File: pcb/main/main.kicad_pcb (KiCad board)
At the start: 2 copper layers, 29.4 x 98.3 mm, 54 parts, among them J1 Conn_01x04, J2 USB_B, J3 Serial, J4 STLink, J5 RJ45, J6 SELECT, J7 READ, J8 TRACKBALL, SW5 RST_SW, SW6 BOOT0, SW7 BOOT1, U1 3.3v regul, U2 STM32F103C8Tx, Y1 32.768kHz, Y2 8MHz

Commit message: fix pcb
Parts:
- removed D5, D6, D7: LED, LED_SMD:LED_1206_3216Metric
- removed G*** (x2): LOGO, folivora:logo
- removed JP10, JP12, JP14, JP16, JP9: R, Jumper:SolderJumper-2_P1.3mm_Open_TrianglePad1.0x1.5mm
- removed JP11, JP13, JP15, JP17: L, Jumper:SolderJumper-2_P1.3mm_Open_TrianglePad1.0x1.5mm
- removed SW5: RST_SW, Button_Switch_THT:SW_Tactile_SPST_Angled_PTS645Vx31-2LFS
- removed SW6: BOOT0, Button_Switch_THT:SW_CuK_OS102011MA1QN1_SPDT_Angled
- removed SW7: BOOT1, Button_Switch_THT:SW_CuK_OS102011MA1QN1_SPDT_Angled
- added C12: C, Capacitor_SMD:C_0402_1005Metric, F.Cu at (25.0, -43.8)
- added C13: 1uF, Capacitor_SMD:C_0402_1005Metric, F.Cu at (12.1, -39.4)
- added C14: 0.1uF, Capacitor_SMD:C_0402_1005Metric, F.Cu at (12.1, -40.6)
- added C15: 0.1uF, Capacitor_SMD:C_0402_1005Metric, F.Cu at (8.26, -36.8)
- added C16: 1uF, Capacitor_SMD:C_0402_1005Metric, F.Cu at (32.4, -46.4)
- added C17: 1uF, Capacitor_SMD:C_0402_1005Metric, F.Cu at (17.1, -8.89)
- added C18: 0.1uF, Capacitor_SMD:C_0402_1005Metric, F.Cu at (17.1, -7.62)
- added C19: 0.1uF, Capacitor_SMD:C_0402_1005Metric, F.Cu at (14.6, -5.08)
- added C20: 1uF, Capacitor_SMD:C_0402_1005Metric, F.Cu at (13.3, -5.08)
- added C21: 0.1uF, Capacitor_SMD:C_0402_1005Metric, F.Cu at (1.91, -34.3)
- added D1: SBD, Diode_SMD:D_SOD-123, F.Cu at (15.9, -36.8)
- added D2: Error, LED_SMD:LED_0603_1608Metric, F.Cu at (1.91, -67.9)
- added D3: Status, LED_SMD:LED_0603_1608Metric, F.Cu at (1.91, -66.0)
- added D4: SBD, Diode_SMD:D_SOD-123, F.Cu at (17.1, -11.4)
- added J10: COL4, Connector_JST:JST_PH_B4B-PH-K_1x04_P2.00mm_Vertical, F.Cu at (28.9, -34.9)
- added J11: COL6, Connector_JST:JST_PH_B3B-PH-K_1x03_P2.00mm_Vertical, F.Cu at (38.9, -34.9)
- added J12: OLED, folivora:OLED, F.Cu at (6.35, -8.89)
- added J13: Conn_01x05_Female, Connector_JST:JST_PH_B5B-PH-K_1x05_P2.00mm_Vertical, F.Cu at (34.9, -11.4)
- added J9: COL3, Connector_JST:JST_PH_B4B-PH-K_1x04_P2.00mm_Vertical, F.Cu at (28.9, -29.2)
- added JP1: OLED_1_F, Jumper:SolderJumper-2_P1.3mm_Open_Pad1.0x1.5mm, F.Cu at (2.54, -12.7)
- added R10: 10k, Resistor_SMD:R_0402_1005Metric, B.Cu at (36.8, -20.3)
- added R11: 10k, Resistor_SMD:R_0402_1005Metric, B.Cu at (34.9, -20.3)
- added R12: 10k, Resistor_SMD:R_0402_1005Metric, B.Cu at (40.6, -26.0)
- added R13: 10k, Resistor_SMD:R_0402_1005Metric, B.Cu at (38.7, -26.0)
- added R14: 10k, Resistor_SMD:R_0402_1005Metric, B.Cu at (36.8, -26.0)
- added R15: 10k, Resistor_SMD:R_0402_1005Metric, B.Cu at (34.9, -26.0)
- added R16: 10k, Resistor_SMD:R_0402_1005Metric, B.Cu at (28.6, -31.8)
- added R17: 10k, Resistor_SMD:R_0402_1005Metric, B.Cu at (26.7, -31.8)
- added R18: 10k, Resistor_SMD:R_0402_1005Metric, B.Cu at (24.8, -31.8)
- added R19: 10k, Resistor_SMD:R_0402_1005Metric, B.Cu at (22.9, -31.8)
- added R20: 10k, Resistor_SMD:R_0402_1005Metric, B.Cu at (34.9, -37.5)
- added R21: 10k, Resistor_SMD:R_0402_1005Metric, B.Cu at (36.8, -37.5)
- added R22: 10k, Resistor_SMD:R_0402_1005Metric, B.Cu at (38.7, -37.5)
- added R23: 10k, Resistor_SMD:R_0402_1005Metric, B.Cu at (22.9, -37.5)
- added R24: 10, Resistor_SMD:R_0402_1005Metric, F.Cu at (20.3, -65.2)
- added R25: 10k, Resistor_SMD:R_0402_1005Metric, B.Cu at (24.8, -37.5)
- added R26: 10k, Resistor_SMD:R_0402_1005Metric, B.Cu at (26.7, -37.5)
- added R27: 10k, Resistor_SMD:R_0402_1005Metric, B.Cu at (28.6, -37.5)
- added R28: 10k, Resistor_SMD:R_0402_1005Metric, B.Cu at (22.9, -26.0)
- added R29: 10k, Resistor_SMD:R_0402_1005Metric, B.Cu at (24.8, -26.0)
- added R30: 10k, Resistor_SMD:R_0402_1005Metric, B.Cu at (26.7, -26.0)
- added R31: 10k, Resistor_SMD:R_0402_1005Metric, B.Cu at (28.6, -26.0)
- added R32: 10k, Resistor_SMD:R_0402_1005Metric, B.Cu at (34.9, -31.8)
- added R33: 10k, Resistor_SMD:R_0402_1005Metric, B.Cu at (36.8, -31.8)
- added R34: 10k, Resistor_SMD:R_0402_1005Metric, B.Cu at (38.7, -31.8)
- added R35: 10k, Resistor_SMD:R_0402_1005Metric, B.Cu at (22.9, -20.3)
- added R36: 10k, Resistor_SMD:R_0402_1005Metric, B.Cu at (24.8, -20.3)
- added R37: 10k, Resistor_SMD:R_0402_1005Metric, B.Cu at (26.7, -20.3)
- added R38: 10k, Resistor_SMD:R_0402_1005Metric, B.Cu at (28.6, -20.3)
- added R39: R, Resistor_SMD:R_0402_1005Metric, F.Cu at (22.9, -3.81)
- added R40: 10, Resistor_SMD:R_0402_1005Metric, F.Cu at (20.3, -64.1)
- added R41: 5.1k, Resistor_SMD:R_0402_1005Metric, F.Cu at (17.8, -69.8)
- added R8: 10k, Resistor_SMD:R_0402_1005Metric, B.Cu at (40.6, -20.3)
- added R9: 10k, Resistor_SMD:R_0402_1005Metric, B.Cu at (38.7, -20.3)
- added REF_M1: MountingHole_2.2mm_M2, MountingHole:MountingHole_2.2mm_M2, F.Cu at (41.9, -2.54)
- added REF_M2: MountingHole_2.2mm_M2, MountingHole:MountingHole_2.2mm_M2, F.Cu at (10.8, -2.54)
- added REF_M3: MountingHole_2.2mm_M2, MountingHole:MountingHole_2.2mm_M2, F.Cu at (2.54, -2.54)
- added REF_M4: MountingHole_2.2mm_M2, MountingHole:MountingHole_2.2mm_M2, F.Cu at (10.8, -45.7)
- added REF_M5: MountingHole_2.2mm_M2, MountingHole:MountingHole_2.2mm_M2, F.Cu at (2.54, -45.7)
- added REF_M6: MountingHole_2.2mm_M2, MountingHole:MountingHole_2.2mm_M2, F.Cu at (41.9, -72.4)
- added REF_M7: MountingHole_2.2mm_M2, MountingHole:MountingHole_2.2mm_M2, F.Cu at (2.54, -72.4)
- added SW1: SW_SPDT, Button_Switch_SMD:SW_SPDT_PCM12, F.Cu at (2.54, -29.2)
- added SW2: SW_SPDT, Button_Switch_SMD:SW_SPDT_PCM12, F.Cu at (2.54, -19.7)
- added SW3: RESET, Button_Switch_SMD:SW_SPST_EVQP7C, F.Cu at (1.91, -38.1)
- added U3: PCA9306DC1, Package_SO:VSSOP-8_2.3x2mm_P0.5mm, F.Cu at (22.9, -1.91)
- added U4: HT7727, Package_TO_SOT_SMD:SOT-23, F.Cu at (17.1, -5.08)
- C1, C2: value 10uF -> 0.1uF; footprint Capacitor_SMD:C_1206_3216Metric_Pad1.42x1.75mm_HandSolder -> Capacitor_SMD:C_0402_1005Metric
- C10, C11, C9: value 0.1uF -> C; footprint Capacitor_SMD:C_0603_1608Metric_Pad1.05x0.95mm_HandSolder -> Capacitor_SMD:C_0402_1005Metric
- C3: value 12.5pF -> 0.1uF; footprint Capacitor_SMD:C_0603_1608Metric_Pad1.05x0.95mm_HandSolder -> Capacitor_SMD:C_0402_1005Metric
- C4: value 12.5pF[ -> 0.1uF; footprint Capacitor_SMD:C_0603_1608Metric_Pad1.05x0.95mm_HandSolder -> Capacitor_SMD:C_0402_1005Metric
- C5: value 20pF -> 0.1uF; footprint Capacitor_SMD:C_0603_1608Metric_Pad1.05x0.95mm_HandSolder -> Capacitor_SMD:C_0402_1005Metric
- C6: value 20pF -> 1uF; footprint Capacitor_SMD:C_0603_1608Metric_Pad1.05x0.95mm_HandSolder -> Capacitor_SMD:C_0402_1005Metric
- C7: value 10uF -> 10nF; footprint Capacitor_SMD:C_0603_1608Metric_Pad1.05x0.95mm_HandSolder -> Capacitor_SMD:C_0402_1005Metric
- C8: value 0.1uF -> 4.7uF; footprint Capacitor_SMD:C_0603_1608Metric_Pad1.05x0.95mm_HandSolder -> Capacitor_SMD:C_0402_1005Metric
- J1: value Conn_01x04 -> USB_C_Receptacle_USB2.0; footprint Connector_PinSocket_2.54mm:PinSocket_1x04_P2.54mm_Vertical -> Connector_USB:USB_C_Receptacle_HRO_TYPE-C-31-M-12
- J2: value USB_B -> RJ45; footprint Connector_USB:USB_B_OST_USB-B1HSxx_Horizontal -> folivora:RJ45_rev
- J3: value Serial -> RJ45; footprint Connector_PinHeader_2.54mm:PinHeader_1x04_P2.54mm_Vertical -> folivora:RJ45_rev; moved to B.Cu
- J4: value STLink -> Pad; footprint Connector_PinHeader_2.54mm:PinHeader_1x04_P2.54mm_Vertical -> Connector_JST:JST_PH_B4B-PH-K_1x04_P2.00mm_Vertical
- J5: value RJ45 -> Thumb; footprint folivora:RJ45_rev -> Connector_JST:JST_PH_B4B-PH-K_1x04_P2.00mm_Vertical
- J6: value SELECT -> COL1; footprint Connector_PinSocket_2.54mm:PinSocket_1x05_P2.54mm_Vertical -> Connector_JST:JST_PH_B4B-PH-K_1x04_P2.00mm_Vertical
- J7: value READ -> COL5; footprint Connector_PinSocket_2.54mm:PinSocket_1x06_P2.54mm_Vertical -> Connector_JST:JST_PH_B3B-PH-K_1x03_P2.00mm_Vertical
- J8: value TRACKBALL -> COL2; footprint Connector_PinSocket_2.54mm:PinSocket_1x06_P2.54mm_Vertical -> Connector_JST:JST_PH_B4B-PH-K_1x04_P2.00mm_Vertical
- JP2: value L -> OLED_1_B; footprint Jumper:SolderJumper-2_P1.3mm_Open_TrianglePad1.0x1.5mm -> Jumper:SolderJumper-2_P1.3mm_Open_Pad1.0x1.5mm
- JP3: value R -> OLED_2_F; footprint Jumper:SolderJumper-2_P1.3mm_Open_TrianglePad1.0x1.5mm -> Jumper:SolderJumper-2_P1.3mm_Open_Pad1.0x1.5mm
- JP4: value L -> OLED_2_B; footprint Jumper:SolderJumper-2_P1.3mm_Open_TrianglePad1.0x1.5mm -> Jumper:SolderJumper-2_P1.3mm_Open_Pad1.0x1.5mm
- JP5: value R -> OLED_3_F; footprint Jumper:SolderJumper-2_P1.3mm_Open_TrianglePad1.0x1.5mm -> Jumper:SolderJumper-2_P1.3mm_Open_Pad1.0x1.5mm
- JP6: value L -> OLED_3_B; footprint Jumper:SolderJumper-2_P1.3mm_Open_TrianglePad1.0x1.5mm -> Jumper:SolderJumper-2_P1.3mm_Open_Pad1.0x1.5mm
- JP7: value R -> OLED_4_F; footprint Jumper:SolderJumper-2_P1.3mm_Open_TrianglePad1.0x1.5mm -> Jumper:SolderJumper-2_P1.3mm_Open_Pad1.0x1.5mm
- JP8: value L -> OLED_4_B; footprint Jumper:SolderJumper-2_P1.3mm_Open_TrianglePad1.0x1.5mm -> Jumper:SolderJumper-2_P1.3mm_Open_Pad1.0x1.5mm
- R1: footprint Resistor_SMD:R_0603_1608Metric -> Resistor_SMD:R_0402_1005Metric
- R2, R3: value R -> 10M; footprint Resistor_SMD:R_0603_1608Metric -> Resistor_SMD:R_0402_1005Metric
- R4: value 10Mohm -> R; footprint Resistor_SMD:R_0603_1608Metric_Pad1.05x0.95mm_HandSolder -> Resistor_SMD:R_0402_1005Metric
- R5, R6, R7: value 10kohm -> R; footprint Resistor_SMD:R_0603_1608Metric_Pad1.05x0.95mm_HandSolder -> Resistor_SMD:R_0402_1005Metric
- U1: value 3.3v regul -> STM32F401RETx; footprint Package_TO_SOT_SMD:TO-252-3_TabPin2 -> Package_QFP:LQFP-64_10x10mm_P0.5mm
- U2: value STM32F103C8Tx -> NATLINEAR XT1861B332MR-G; footprint Package_QFP:LQFP-48_7x7mm_P0.5mm -> Package_TO_SOT_SMD:SOT-23
- Y1: value 32.768kHz -> Crystal_8MHz; footprint Crystal:Crystal_SMD_3215-2Pin_3.2x1.5mm -> Crystal:Crystal_SMD_2520-4Pin_2.5x2.0mm
- Y2: value 8MHz -> Crystal_32.768MHz; footprint Crystal:Crystal_SMD_Abracon_ABM3-2Pin_5.0x3.2mm -> Crystal:Crystal_SMD_2520-4Pin_2.5x2.0mm
- moved R5 153.8 mm to (4.45, -67.9), turned to 180 degrees
- moved C7 137.6 mm to (30.3, -46.4), turned to 180 degrees
- moved J1 135.9 mm to (11.4, -70.5), turned to 180 degrees
- moved R6 124.0 mm to (4.45, -66.0), turned to 180 degrees
- moved R1 120.9 mm to (3.17, -42.5)
- moved R2 117.9 mm to (28.2, -46.1), turned to 0 degrees
- moved R3 115.6 mm to (22.5, -46.4), turned to 0 degrees
- moved C8 113.0 mm to (37.5, -57.0)
- moved C11 102.9 mm to (19.9, -43.8), turned to 90 degrees
- moved C2 98.1 mm to (24.8, -61.6), turned to 0 degrees
- moved C5 94.9 mm to (21.0, -50.0), turned to 90 degrees
- moved C3 94.6 mm to (36.2, -50.8), turned to 270 degrees
- moved C1 93.5 mm to (36.2, -57.8), turned to 270 degrees
- moved C10 92.9 mm to (31.0, -43.8)
- moved J5 92.9 mm to (40.9, -17.8), turned to 180 degrees
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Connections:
- C1 pad 1: +5V -> +3V3
- C10 pad 1: +3V3 -> /XTAL1B
- C11 pad 1: +3V3 -> /XTAL2A
- C3 pad 1: GND -> +3V3
- C3 pad 2: /XTAL_C -> GND
- C4 pad 1: GND -> +3V3
- C4 pad 2: /XTAL_D -> GND
- C5 pad 1: GND -> +3V3
- C5 pad 2: /XTAL_A -> GND
- C6 pad 1: GND -> +3V3
- C6 pad 2: /XTAL_B -> GND
- C7 pad 1: /RST -> +3V3
- C8 pad 1: +3V3 -> Net-(C8-Pad1)
- C9 pad 1: +3V3 -> /XTAL1A
- J2 pad 1: /USB_1 -> /SCLK
- J2 pad 2: /USB_2 -> /MISO
- J2 pad 3: /USB_3 -> /MOSI
- J2 pad 4: /USB_4 -> VBUS
- J2 pad 5: GND -> VBUS
- J3 pad 1: GND -> /SCLK
- J3 pad 2: /RX -> /MOSI
- J3 pad 3: /TX -> /MISO
- J3 pad 4: +3V3 -> VBUS
- J4 pad 1: GND -> Net-(J4-Pad1)
- J4 pad 2: /SWCLK -> Net-(J4-Pad2)
- J4 pad 3: /SWDIO -> Net-(J4-Pad3)
- J4 pad 4: +3V3 -> Net-(J4-Pad4)
- J5 pad 1: GND -> Net-(J5-Pad1)
- J5 pad 2: GND -> Net-(J5-Pad2)
- J5 pad 3: /SCK -> Net-(J5-Pad3)
- J5 pad 4: /MOSI -> Net-(J5-Pad4)
- J6 pad 1: /SELECT0 -> Net-(J6-Pad1)
- J6 pad 2: /SELECT1 -> Net-(J6-Pad2)
- J6 pad 3: /SELECT2 -> Net-(J6-Pad3)
- J6 pad 4: /SELECT3 -> Net-(J6-Pad4)
- J7 pad 1: /READ0 -> Net-(J7-Pad1)
- J7 pad 2: /READ1 -> Net-(J7-Pad2)
- J7 pad 3: /READ2 -> Net-(J7-Pad3)
- J8 pad 1: +3V3 -> Net-(J8-Pad1)
- J8 pad 2: /UP -> Net-(J8-Pad2)
- J8 pad 3: /DOWN -> Net-(J8-Pad3)
- J8 pad 4: /RIGHT -> Net-(J8-Pad4)
- JP2 pad 1: /D- -> /SDA
- JP2 pad 2: /USB_1 -> /OLED1
- JP3 pad 1: +5V -> +3V3
- JP3 pad 2: /USB_1 -> /OLED2
- JP4 pad 1: +5V -> /SCL
- JP4 pad 2: /USB_2 -> /OLED2
- JP5 pad 1: /D- -> /SCL
- JP5 pad 2: /USB_2 -> /OLED3
- JP6 pad 1: GND -> +3V3
- JP6 pad 2: /USB_3 -> /OLED3
- JP7 pad 1: /D+ -> /SDA
- JP7 pad 2: /USB_3 -> /OLED4
- JP8 pad 1: /D+ -> GND
- JP8 pad 2: /USB_4 -> /OLED4
- R1 pad 2: Net-(D5-Pad2) -> Net-(C21-Pad2)
- R2 pad 1: +3V3 -> /XTAL1A
- R2 pad 2: Net-(D6-Pad2) -> /XTAL1B
- R3 pad 1: +3V3 -> /XTAL2A
- R3 pad 2: Net-(D7-Pad2) -> /XTAL2B
- R4 pad 1: /XTAL_B -> +3V3
- R4 pad 2: /XTAL_A -> Net-(R4-Pad2)
- R5 pad 1: /RST -> +3V3
- R5 pad 2: +3V3 -> Net-(D2-Pad2)
- R6 pad 1: Net-(R6-Pad1) -> +3V3
- R6 pad 2: /BOOT0 -> Net-(D3-Pad2)
- R7 pad 1: Net-(R7-Pad1) -> +3V3
- R7 pad 2: /BOOT1 -> Net-(R7-Pad2)
- U1 pad 1: +5V -> +3V3
- U1 pad 2: GND -> /XTAL2A
- U1 pad 3: +3V3 -> /XTAL2B
- U2 pad 1: +3V3 -> VBUS
- U2 pad 2: Net-(U2-Pad2) -> GND
- U2 pad 3: /XTAL_C -> +3V3
- Y1 pad 1: /XTAL_D -> /XTAL1B
- Y1 pad 2: /XTAL_C -> GND
- Y2 pad 1: /XTAL_B -> /XTAL2B
- Y2 pad 2: /XTAL_A -> GND
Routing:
- net +3V3: track 175.5 -> 265.0 mm, vias 7 -> 3
- net VBUS: track 0.00 -> 85.0 mm
- net Net-(J5-Pad3): track 0.00 -> 71.3 mm, vias 0 -> 1
- net Net-(J5-Pad2): track 0.00 -> 69.3 mm, vias 0 -> 1
- net Net-(J5-Pad1): track 0.00 -> 61.9 mm, vias 0 -> 1
- net Net-(J5-Pad4): track 0.00 -> 61.8 mm
- net /SDA: track 22.1 -> 80.4 mm
- net /SCL: track 17.7 -> 75.3 mm
- net Net-(J7-Pad3): track 0.00 -> 54.1 mm, vias 0 -> 2
- net Net-(J7-Pad2): track 0.00 -> 50.7 mm, vias 0 -> 2
- net Net-(J4-Pad1): track 0.00 -> 50.4 mm
- net Net-(J4-Pad2): track 0.00 -> 50.2 mm
- net Net-(J4-Pad3): track 0.00 -> 49.6 mm
- net Net-(J8-Pad3): track 0.00 -> 46.5 mm, vias 0 -> 1
- net /RST: track 45.7 -> 0.00 mm, vias 2 -> 0
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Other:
- board size 29.4 x 98.3 mm -> 44.5 x 74.9 mm

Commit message: pcb update
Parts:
- removed JP1: OLED_1_F, Jumper:SolderJumper-2_P1.3mm_Open_Pad1.0x1.5mm
- removed JP2: OLED_1_B, Jumper:SolderJumper-2_P1.3mm_Open_Pad1.0x1.5mm
- removed JP3: OLED_2_F, Jumper:SolderJumper-2_P1.3mm_Open_Pad1.0x1.5mm
- removed JP4: OLED_2_B, Jumper:SolderJumper-2_P1.3mm_Open_Pad1.0x1.5mm
- removed JP5: OLED_3_F, Jumper:SolderJumper-2_P1.3mm_Open_Pad1.0x1.5mm
- removed JP6: OLED_3_B, Jumper:SolderJumper-2_P1.3mm_Open_Pad1.0x1.5mm
- removed JP7: OLED_4_F, Jumper:SolderJumper-2_P1.3mm_Open_Pad1.0x1.5mm
- removed JP8: OLED_4_B, Jumper:SolderJumper-2_P1.3mm_Open_Pad1.0x1.5mm
- added J14: OLED, folivora:OLED, F.Cu at (6.35, -8.89)
- J12: moved to B.Cu
- R10, R11, R12, R13, R14, R15, R16, R17, R18, R19, R20, R21, R22, R23, R25, R26, R27, R28, R29, R30, R31, R32, R33, R34, R35, R36, R37, R38, R8, R9: moved to F.Cu
- moved C16 6.90 mm to (37.0, -51.5)
- moved C12 6.90 mm to (29.6, -48.9)
- moved C4 6.90 mm to (27.5, -53.4)
- moved C5 6.90 mm to (25.6, -55.1)
- moved C9 6.90 mm to (30.7, -48.9)
- moved R3 6.90 mm to (27.1, -51.5)
- moved Y1 6.90 mm to (33.2, -48.9)
- moved Y2 6.90 mm to (27.1, -48.9)
- moved C1 6.90 mm to (40.8, -62.9)
- moved C10 6.90 mm to (35.6, -48.9)
- moved C3 6.90 mm to (40.8, -55.9)
- moved C8 6.90 mm to (42.1, -62.1)
- moved C7 6.90 mm to (34.9, -51.5)
- moved R2 6.90 mm to (32.8, -51.2)
- moved U1 6.90 mm to (33.2, -59.1)
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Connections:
- J1 pad A8: Net-(J1-PadA8) -> (no net)
- J1 pad B8: Net-(J1-PadB8) -> (no net)
- J12 pad 1: /OLED1 -> GND
- J12 pad 2: /OLED2 -> +3V3
- J12 pad 3: /OLED3 -> /SCL
- J12 pad 4: /OLED4 -> /SDA
- J13 pad 3: Net-(J13-Pad3) -> (no net)
- U1 pad 24: Net-(U1-Pad24) -> (no net)
- U1 pad 4: Net-(U1-Pad4) -> (no net)
- U1 pad 41: /TSS -> (no net)
- U1 pad 54: Net-(U1-Pad54) -> (no net)
- U1 pad 57: Net-(U1-Pad57) -> (no net)
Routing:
- net +3V3: track 265.0 -> 345.4 mm, vias 3 -> 8
- net /CONFIG: track 44.8 -> 70.8 mm
- net Net-(J9-Pad2): track 20.8 -> 39.2 mm
- net /SDA: track 80.4 -> 97.4 mm
- net Net-(J9-Pad1): track 22.5 -> 38.6 mm, vias 2 -> 1
- net Net-(J10-Pad4): track 30.6 -> 46.1 mm, vias 1 -> 2
- net Net-(J6-Pad3): track 37.1 -> 52.1 mm, vias 0 -> 1
- net Net-(J9-Pad4): track 25.0 -> 39.7 mm
- net Net-(J11-Pad3): track 32.1 -> 46.6 mm
- net Net-(J6-Pad4): track 45.1 -> 59.3 mm, vias 0 -> 1
- net Net-(J8-Pad1): track 38.7 -> 52.6 mm, vias 2 -> 1
- net Net-(J7-Pad3): track 54.1 -> 67.6 mm, vias 2 -> 1
- net Net-(J6-Pad2): track 39.2 -> 51.0 mm, vias 0 -> 1
- net Net-(J4-Pad4): track 36.8 -> 48.5 mm, vias 0 -> 1
- net /MISO: track 49.5 -> 60.3 mm
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
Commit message: redesign pcb
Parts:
- removed J10: COL4, Connector_JST:JST_PH_B4B-PH-K_1x04_P2.00mm_Vertical
- removed J11: COL6, Connector_JST:JST_PH_B3B-PH-K_1x03_P2.00mm_Vertical
- removed J7: COL5, Connector_JST:JST_PH_B3B-PH-K_1x03_P2.00mm_Vertical
- removed J8: COL2, Connector_JST:JST_PH_B4B-PH-K_1x04_P2.00mm_Vertical
- removed J9: COL3, Connector_JST:JST_PH_B4B-PH-K_1x04_P2.00mm_Vertical
- removed R10, R11, R12, R13, R14, R15, R16, R17, R18, R19, R20, R21, R22, R23, R25, R26, R27, R28, R29, R30, R31, R32, R33, R34, R35, R36, R37, R38, R8, R9: 10k, Resistor_SMD:R_0402_1005Metric
- removed R3: 10M, Resistor_SMD:R_0402_1005Metric
- removed REF_M7: MountingHole_2.2mm_M2, MountingHole:MountingHole_2.2mm_M2
- added C22: 0.1uF, Capacitor_SMD:C_0402_1005Metric, F.Cu at (6.35, -24.8)
- added C23: 0.1uF, Capacitor_SMD:C_0402_1005Metric, F.Cu at (5.24, -34.3)
- added C24: 0.1uF, Capacitor_SMD:C_0402_1005Metric, F.Cu at (27.9, -3.81)
- added C25: 0.1uF, Capacitor_SMD:C_0402_1005Metric, F.Cu at (21.6, -3.17)
- added D5: LED_USB, LED_SMD:LED_0603_1608Metric, F.Cu at (7.24, -46.4)
- added F1: Polyfuse, Fuse:Fuse_0603_1608Metric, F.Cu at (14.6, -29.8)
- added REF_M1: MountingHole_2.2mm_M2, MountingHole:MountingHole_2.2mm_M2, F.Cu at (17.8, -31.1)
- added REF_M1: MountingHole_2.2mm_M2, MountingHole:MountingHole_2.2mm_M2, F.Cu at (17.8, -2.54)
- J13: value Conn_01x05_Female -> trackball
- J4: value Pad -> STLink; footprint Connector_JST:JST_PH_B4B-PH-K_1x04_P2.00mm_Vertical -> Connector_PinHeader_1.27mm:PinHeader_2x07_P1.27mm_Vertical
- J5: value Thumb -> ROW; footprint Connector_JST:JST_PH_B4B-PH-K_1x04_P2.00mm_Vertical -> Connector_JST:JST_PH_B5B-PH-K_1x05_P2.00mm_Vertical
- J6: value COL1 -> COL; footprint Connector_JST:JST_PH_B4B-PH-K_1x04_P2.00mm_Vertical -> Connector_JST:JST_PH_B6B-PH-K_1x06_P2.00mm_Vertical
- R2: value 10M -> R; footprint Resistor_SMD:R_0402_1005Metric -> Resistor_SMD:R_0201_0603Metric_Pad0.64x0.40mm_HandSolder
- moved C12 41.0 mm to (26.0, -8.10), turned to 180 degrees
- moved C4 40.8 mm to (29.1, -12.6)
- moved C9 40.3 mm to (30.9, -8.59), turned to 270 degrees
- moved C10 39.7 mm to (35.8, -9.23)
- moved Y1 39.7 mm to (33.4, -9.23)
- moved C16 39.6 mm to (15.5, -18.2), turned to 180 degrees
- moved C1 39.1 mm to (41.0, -23.8)
- moved C3 39.1 mm to (41.0, -16.8)
- moved C5 39.1 mm to (25.7, -16.0)
- moved C7 39.1 mm to (35.1, -12.4)
- moved C8 39.1 mm to (42.2, -23.0)
- moved C2 39.1 mm to (29.5, -27.6)
- moved U1 39.1 mm to (33.4, -20.0)
- moved Y2 38.3 mm to (26.0, -10.6), turned to 90 degrees
- moved C6 36.1 mm to (35.1, -11.4), turned to 180 degrees
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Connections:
- C13 pad 1: VBUS -> Net-(C13-Pad1)
- C14 pad 1: VBUS -> Net-(C13-Pad1)
- C17 pad 1: VBUS -> Net-(C13-Pad1)
- C18 pad 1: VBUS -> Net-(C13-Pad1)
- C21 pad 2: Net-(C21-Pad2) -> /NRST
- D1 pad 1: VBUS -> Net-(C13-Pad1)
- D4 pad 1: VBUS -> Net-(C13-Pad1)
- J4 pad 1: Net-(J4-Pad1) -> (no net)
- J4 pad 2: Net-(J4-Pad2) -> (no net)
- J4 pad 3: Net-(J4-Pad3) -> +3V3
- J4 pad 4: Net-(J4-Pad4) -> /SWDIO
- J5 pad 1: Net-(J5-Pad1) -> /ROW1
- J5 pad 2: Net-(J5-Pad2) -> /ROW2
- J5 pad 3: Net-(J5-Pad3) -> /ROW3
- J5 pad 4: Net-(J5-Pad4) -> /ROW4
- J6 pad 1: Net-(J6-Pad1) -> /COL1
- J6 pad 2: Net-(J6-Pad2) -> /COL2
- J6 pad 3: Net-(J6-Pad3) -> /COL3
- J6 pad 4: Net-(J6-Pad4) -> /COL4
- R1 pad 2: Net-(C21-Pad2) -> /NRST
- R2 pad 1: /XTAL1A -> VBUS
- R2 pad 2: /XTAL1B -> Net-(D5-Pad2)
- SW2 pad 2: /CONFIG -> /BOOT1
- SW3 pad 2: Net-(C21-Pad2) -> /NRST
- U1 pad 10: Net-(J9-Pad2) -> (no net)
- U1 pad 11: Net-(J9-Pad1) -> (no net)
- U1 pad 14: Net-(J6-Pad1) -> (no net)
- U1 pad 15: Net-(J6-Pad2) -> (no net)
- U1 pad 16: Net-(J6-Pad3) -> /TX
- U1 pad 17: Net-(J6-Pad4) -> /RX
- U1 pad 20: /SS -> (no net)
- U1 pad 21: /SCLK -> (no net)
- U1 pad 22: /MISO -> (no net)
- U1 pad 23: /MOSI -> (no net)
- U1 pad 25: Net-(J4-Pad4) -> (no net)
- U1 pad 26: Net-(J8-Pad1) -> (no net)
- U1 pad 27: Net-(J8-Pad2) -> (no net)
- U1 pad 28: Net-(J8-Pad3) -> /BOOT1
- U1 pad 29: Net-(J10-Pad3) -> (no net)
- U1 pad 33: Net-(J10-Pad4) -> /ROW1
- U1 pad 34: Net-(J11-Pad1) -> /ROW2
- U1 pad 35: Net-(J11-Pad2) -> /ROW3
- U1 pad 36: Net-(J11-Pad3) -> /ROW4
- U1 pad 37: Net-(J4-Pad3) -> /ROW5
- U1 pad 38: Net-(J4-Pad2) -> /COL1
- U1 pad 39: Net-(J4-Pad1) -> /COL2
- U1 pad 40: Net-(J5-Pad4) -> /COL3
- U1 pad 41: (no net) -> /COL4
- U1 pad 42: /LED_ERROR -> /COL5
- U1 pad 43: /LED_STATUS -> /COL6
- U1 pad 46: Net-(J7-Pad1) -> /SWDIO
- U1 pad 49: Net-(J7-Pad2) -> /SWCLK
- U1 pad 50: Net-(J7-Pad3) -> /SS
- U1 pad 51: Net-(J5-Pad3) -> /SCLK
- U1 pad 52: Net-(J5-Pad2) -> /MISO
- U1 pad 53: Net-(J5-Pad1) -> /MOSI
- U1 pad 55: Net-(J8-Pad4) -> /SWO
- U1 pad 56: /CONFIG -> /LED_ERROR
- U1 pad 57: (no net) -> /LED_STATUS
- U1 pad 61: Net-(J10-Pad1) -> (no net)
- U1 pad 62: Net-(J10-Pad2) -> (no net)
- U1 pad 7: Net-(C21-Pad2) -> /NRST
- U1 pad 8: Net-(J9-Pad4) -> (no net)
- U1 pad 9: Net-(J9-Pad3) -> (no net)
- U2 pad 1: VBUS -> Net-(C13-Pad1)
- U4 pad 1: VBUS -> Net-(C13-Pad1)
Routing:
- net +3V3: track 345.4 -> 191.7 mm, vias 8 -> 18
- net /NRST: track 0.00 -> 97.7 mm, vias 0 -> 4
- net /CONFIG: track 70.8 -> 0.00 mm, vias 2 -> 0
- net Net-(J5-Pad4): track 68.4 -> 0.00 mm, vias 1 -> 0
- net Net-(J5-Pad1): track 68.2 -> 0.00 mm, vias 1 -> 0
- net Net-(J7-Pad3): track 67.6 -> 0.00 mm, vias 1 -> 0
- net Net-(J5-Pad3): track 64.5 -> 0.00 mm
- net Net-(J5-Pad2): track 61.0 -> 0.00 mm, vias 1 -> 0
- net Net-(J6-Pad4): track 59.3 -> 0.00 mm, vias 1 -> 0
- net Net-(J4-Pad2): track 57.7 -> 0.00 mm
- net Net-(J4-Pad1): track 57.6 -> 0.00 mm
- net Net-(J4-Pad3): track 56.7 -> 0.00 mm
- net Net-(J8-Pad2): track 53.9 -> 0.00 mm, vias 1 -> 0
- net Net-(J8-Pad3): track 53.7 -> 0.00 mm, vias 1 -> 0
- net Net-(J8-Pad1): track 52.6 -> 0.00 mm, vias 1 -> 0
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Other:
- board size 44.5 x 74.9 mm -> 50.8 x 52.7 mm

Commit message: finish
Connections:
- J2 pad 1: /SCLK -> /MISO
- J2 pad 4: VBUS -> /SCLK
- J2 pad 6: /SS -> /MOSI
- J2 pad 7: GND -> /SS
- J3 pad 1: /SCLK -> /MISO
- J3 pad 2: /MOSI -> /MISO
- J3 pad 3: /MISO -> /MOSI
- J3 pad 4: VBUS -> /SCLK
- J3 pad 6: /SS -> /MOSI
- J3 pad 7: GND -> /SS
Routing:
- net /SCLK: track 31.1 -> 16.8 mm, vias 2 -> 1
- net /SS: track 20.8 -> 29.0 mm, vias 2 -> 1
- net /MOSI: track 34.5 -> 28.0 mm, vias 3 -> 5
- net GND: track 282.7 -> 288.0 mm
- net /MISO: track 33.7 -> 30.0 mm, vias 2 -> 1
- net VBUS: track 54.6 -> 55.4 mm
- net /SWO: track 41.6 -> 42.2 mm

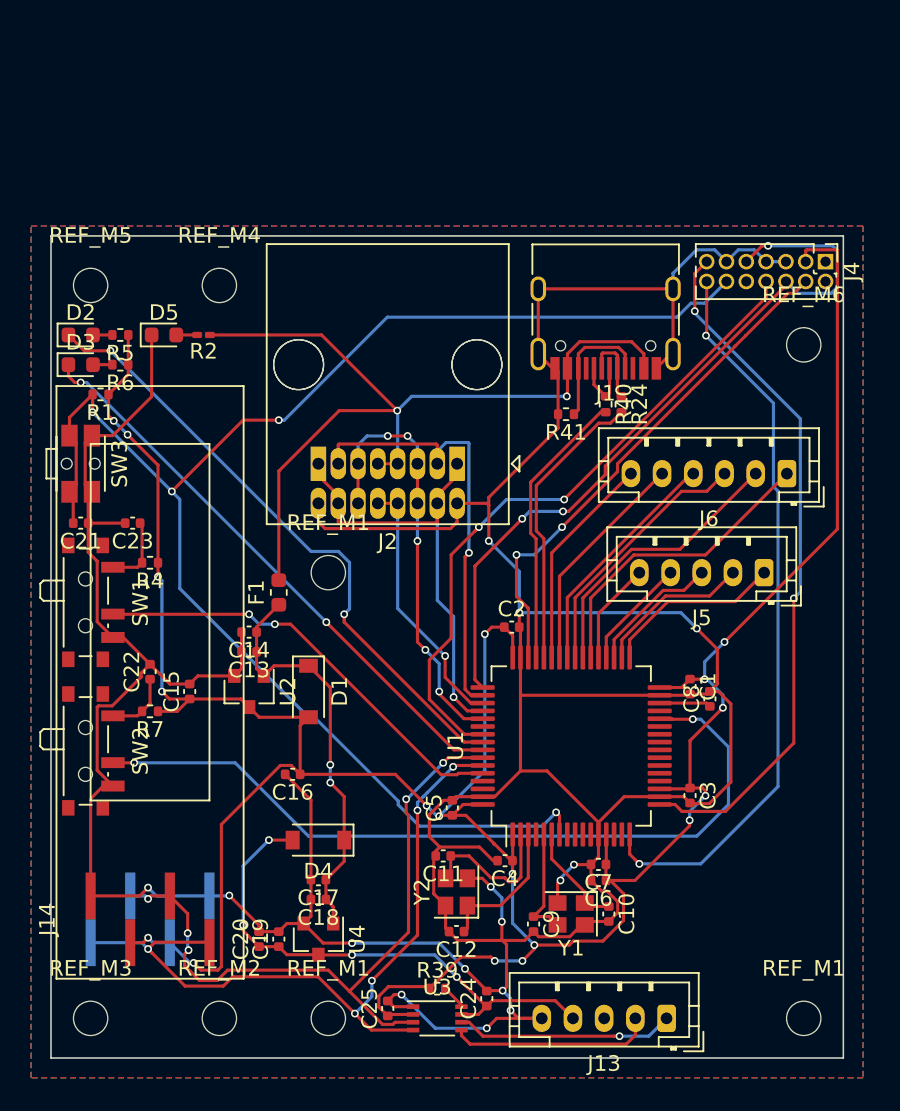
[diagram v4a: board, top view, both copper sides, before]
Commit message: fix RJ45 placing
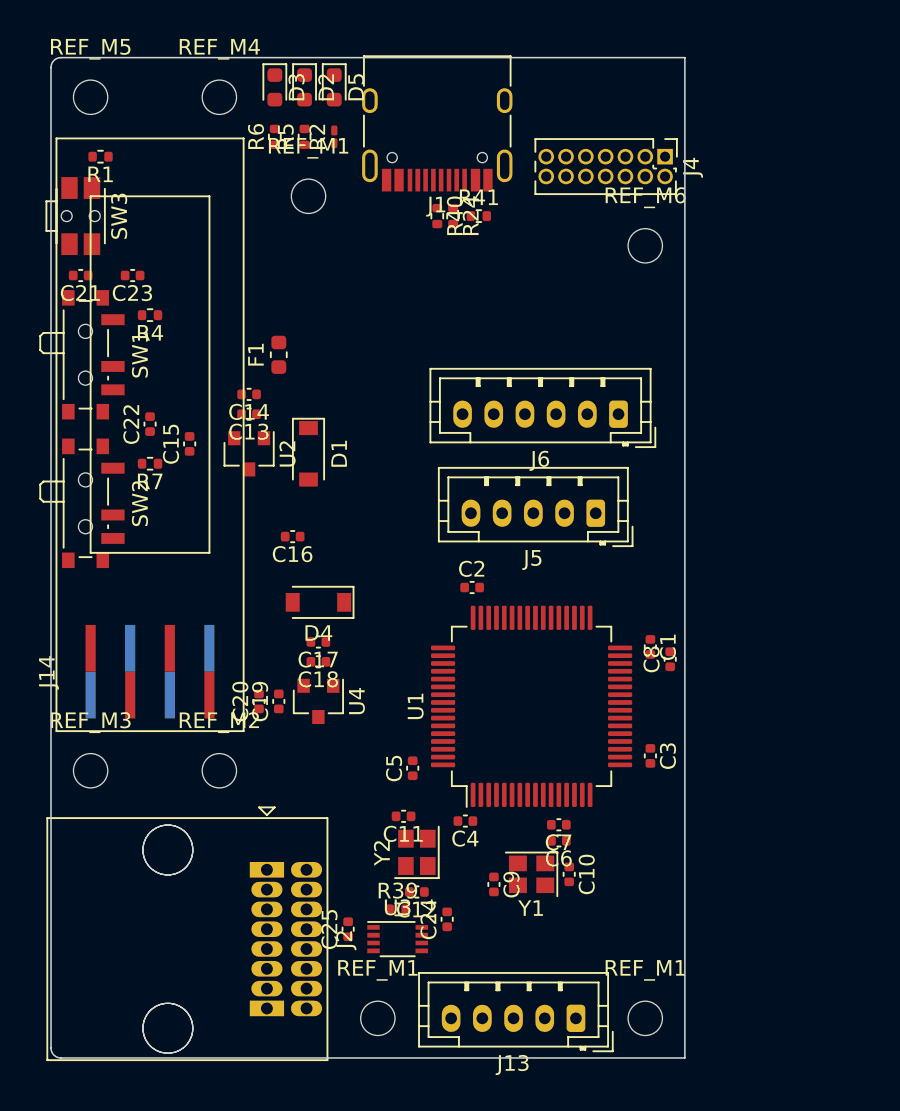
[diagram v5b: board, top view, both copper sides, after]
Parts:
- moved J3 35.1 mm to (13.8, -3.17), turned to 90 degrees
- moved J2 28.7 mm to (13.8, -12.1), turned to 270 degrees
- moved REF_M1 24.2 mm to (16.5, -55.2)
- moved D3 21.7 mm to (14.4, -62.2), turned to 270 degrees
- moved D2 21.4 mm to (16.3, -62.2), turned to 270 degrees
- moved D5 19.3 mm to (18.2, -62.2), turned to 270 degrees
- moved R6 17.6 mm to (14.4, -59.1), turned to 90 degrees
- moved R5 17.3 mm to (16.3, -59.1), turned to 90 degrees
- moved J1 16.2 mm to (24.8, -60.3)
- moved R24 16.2 mm to (25.8, -54.0)
- moved R40 16.2 mm to (24.8, -54.0)
- moved SW2 15.9 mm to (2.54, -35.6)
- moved C21 15.9 mm to (1.91, -50.2)
- moved C22 15.9 mm to (6.35, -40.6)
- moved C23 15.9 mm to (5.24, -50.2)
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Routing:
- net GND: track 288.0 -> 0.00 mm, vias 15 -> 0
- net +3V3: track 191.7 -> 0.00 mm, vias 18 -> 0
- net /NRST: track 97.7 -> 0.00 mm, vias 4 -> 0
- net VBUS: track 55.4 -> 0.00 mm, vias 2 -> 0
- net /BOOT1: track 51.1 -> 0.00 mm, vias 2 -> 0
- net /SWCLK: track 48.5 -> 0.00 mm, vias 3 -> 0
- net /SDA: track 48.0 -> 0.00 mm, vias 5 -> 0
- net /TX: track 47.4 -> 0.00 mm, vias 2 -> 0
- net /RX: track 44.8 -> 0.00 mm, vias 2 -> 0
- net /SCL: track 44.5 -> 0.00 mm, vias 5 -> 0
- net /SWO: track 42.2 -> 0.00 mm, vias 2 -> 0
- net /LED_ERROR: track 40.1 -> 0.00 mm, vias 2 -> 0
- net /LED_STATUS: track 37.2 -> 0.00 mm, vias 2 -> 0
- net +2V8: track 33.6 -> 0.00 mm, vias 4 -> 0
- net /SWDIO: track 33.0 -> 0.00 mm, vias 2 -> 0
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- removed copper zone on B.Cu, net GND
- removed copper zone on F.Cu, net GND
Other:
- board size 50.8 x 52.7 mm -> 40.6 x 64.1 mm

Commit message: fix connector
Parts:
- R2: footprint Resistor_SMD:R_0201_0603Metric_Pad0.64x0.40mm_HandSolder -> Resistor_SMD:R_0402_1005Metric
- moved C25 0.46 mm to (19.4, -8.51)
- moved C4 0.06 mm to (26.5, -15.2)
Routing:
- net GND: track 0.00 -> 265.8 mm, vias 0 -> 14
- net +3V3: track 0.00 -> 178.3 mm, vias 0 -> 11
- net /NRST: track 0.00 -> 85.9 mm, vias 0 -> 7
- net VBUS: track 0.00 -> 67.9 mm, vias 0 -> 3
- net /SWCLK: track 0.00 -> 47.8 mm, vias 0 -> 5
- net /LED_STATUS: track 0.00 -> 47.3 mm, vias 0 -> 6
- net /RX: track 0.00 -> 46.7 mm, vias 0 -> 2
- net /TX: track 0.00 -> 46.4 mm, vias 0 -> 1
- net /LED_ERROR: track 0.00 -> 45.8 mm, vias 0 -> 6
- net /SCL: track 0.00 -> 45.6 mm, vias 0 -> 1
- net /MISO: track 0.00 -> 45.5 mm, vias 0 -> 1
- net +2V8: track 0.00 -> 44.1 mm, vias 0 -> 4
- net /SWO: track 0.00 -> 42.8 mm, vias 0 -> 8
- net /SDA: track 0.00 -> 40.7 mm, vias 0 -> 3
- net /BOOT1: track 0.00 -> 40.3 mm, vias 0 -> 2
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- added copper zone on B.Cu, net GND
- added copper zone on F.Cu, net GND
